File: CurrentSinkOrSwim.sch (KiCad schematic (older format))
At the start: 6 parts

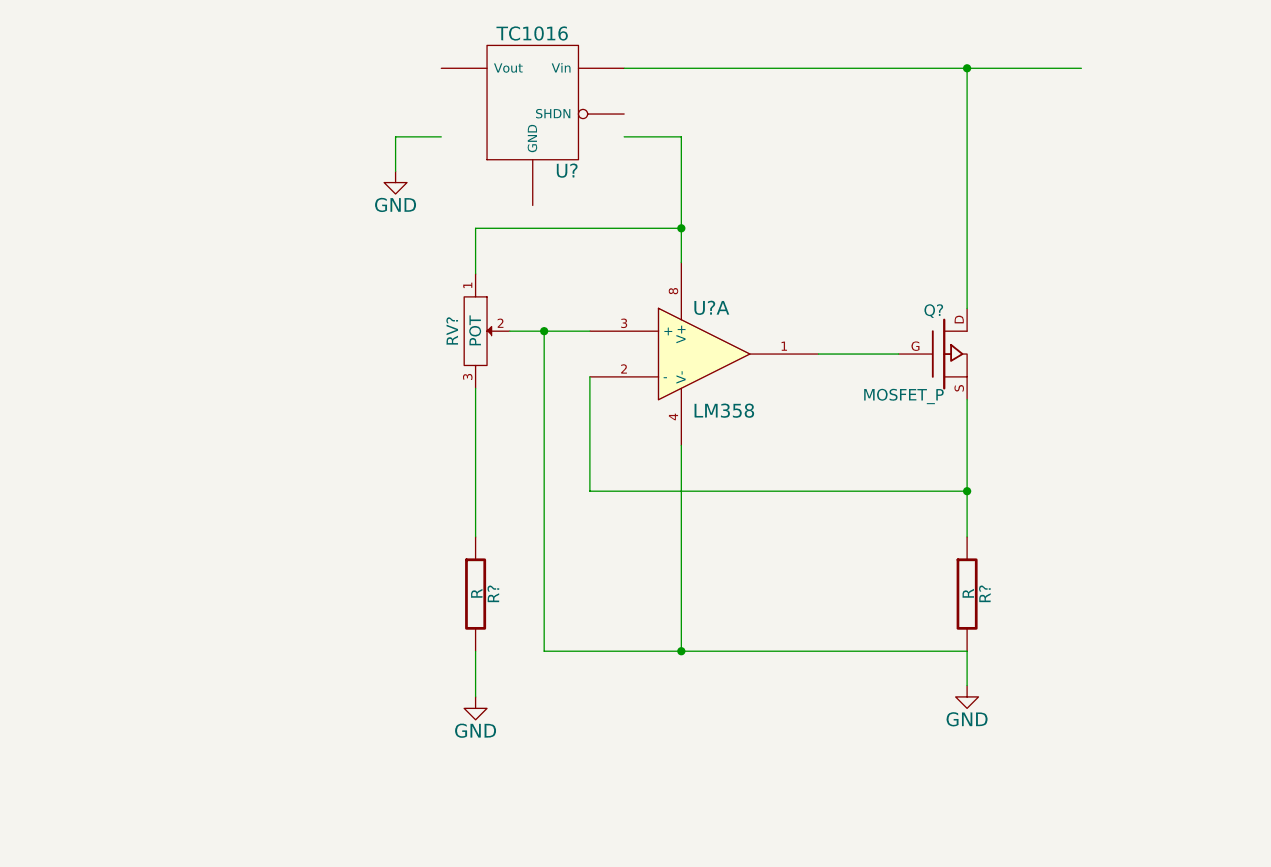
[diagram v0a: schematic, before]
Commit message: Corrections to schematic and .gitignore
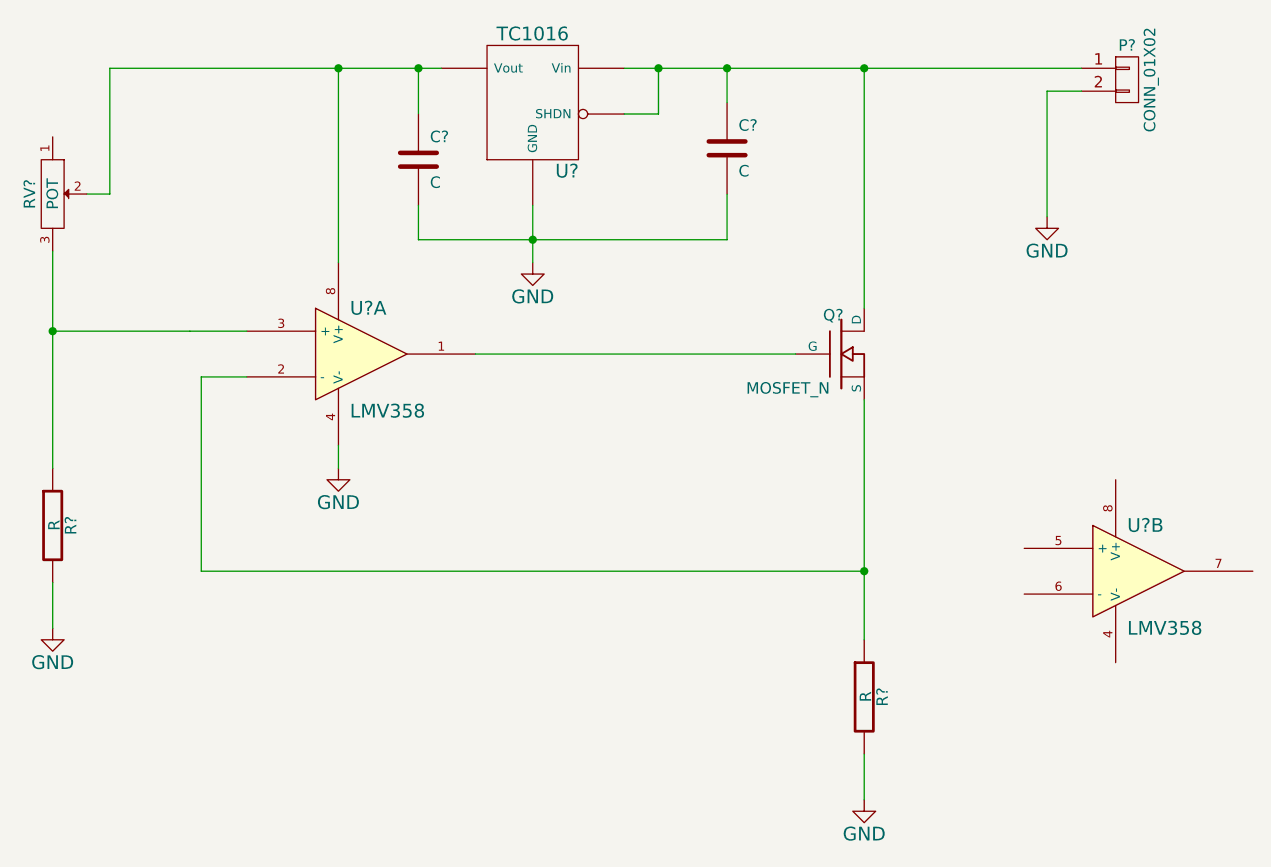
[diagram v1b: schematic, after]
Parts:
- removed Q?: MOSFET_P, symbol MOSFET_P
- removed U?: LM358, symbol LM358
- removed U?: TC1016, symbol TC1016
- added C? (x2): C, symbol C
- added P?: CONN_01X02, symbol CONN_01X02
- added Q?: MOSFET_N, symbol MOSFET_N
- added U? (x2): LMV358, symbol LMV358
- added U?: TC1016, symbol TC1016
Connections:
- wire segments 24 -> 37
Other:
- moved on the sheet: R?, RV?

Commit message: Small adjustments
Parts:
- added C?: C, symbol C
- added R?: 0, symbol R
- Q?: value MOSFET_N -> BUK9575; MPN (none) -> BUK9575-100A,127
- R?: value R -> .1; MPN (none) -> AC01000001007JA100
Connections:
- net GND: now also C?.2
- net 2.7v: now reaches C?.1, RV?.2, U?.4 (Vout), U?.8 (V+)
- net 2.7v: now also C?.1
- net at C?.1, P?.1 (P1), Q?.D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: now also R?.1; no longer U?.1 (SHDN)
- new net: R?.2, U?.1 (SHDN)
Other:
- moved on the sheet: C?, P?, R?, RV?, U?
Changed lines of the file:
@@
 L R R?
 U 1 1 54CE76B8
-P 2400 3800
-F 0 "R?" V 2480 3800 50  0000 C CNN
-F 1 "R" V 2407 3801 50  0000 C CNN
-F 2 "" V 2330 3800 30  0000 C CNN
-F 3 "" H 2400 3800 30  0000 C CNN
-	1    2400 3800
+P 2400 3850
+F 0 "R?" V 2480 3850 50  0000 C CNN
+F 1 "R" V 2407 3851 50  0000 C CNN
+F 2 "" V 2330 3850 30  0000 C CNN
+F 3 "" H 2400 3850 30  0000 C CNN
+	1    2400 3850
 	1    0    0    -1
 $EndComp
@@
 P 5950 4550
 F 0 "R?" V 6030 4550 50  0000 C CNN
-F 1 "R" V 5957 4551 50  0000 C CNN
+F 1 ".1" V 5957 4551 50  0000 C CNN
 F 2 "" V 5880 4550 30  0000 C CNN
 F 3 "" H 5950 4550 30  0000 C CNN
+F 4 "AC01000001007JA100" V 5950 4550 60  0001 C CNN "MPN"
 	1    5950 4550
 	1    0    0    -1
-$EndComp
-Wire Wire Line
-	4250 3050 5650 3050
-Wire Wire Line
-	5950 3250 5950 4000
-Wire Wire Line
-	5950 4000 5950 4300
-Wire Wire Line
-	2400 2600 2400 2950
-Wire Wire Line
-	2400 2950 2400 3550
-$Comp
-L POT RV?
-U 1 1 54CE7B4E
-P 2400 2350
-F 0 "RV?" H 2400 2250 50  0000 C CNN
-F 1 "POT" H 2400 2350 50  0000 C CNN
-F 2 "" H 2400 2350 60  0000 C CNN
-F 3 "" H 2400 2350 60  0000 C CNN
-	1    2400 2350
-	0    1    1    0
 $EndComp
 $Comp
@@
 	1    0    0    -1
 $EndComp
-Wire Wire Line
-	2400 4050 2400 4250
-Wire Wire Line
-	5950 4800 5950 5000
-Wire Wire Line
-	3050 4000 5950 4000
-Connection ~ 5950 4000
-Wire Wire Line
-	4900 1800 5050 1800
-Wire Wire Line
-	5050 1800 5350 1800
-Wire Wire Line
-	5350 1800 5950 1800
-Wire Wire Line
-	5950 1800 6900 1800
-Wire Wire Line
-	5950 1800 5950 2850
-Connection ~ 5950 1800
 $Comp
 L LMV358 U?
@@
 P 5850 3050
 F 0 "Q?" H 5860 3220 50  0000 R CNN
-F 1 "MOSFET_N" H 5800 2900 50  0000 R CNN
+F 1 "BUK9575" H 5800 2900 50  0000 R CNN
 F 2 "" H 5850 3050 60  0000 C CNN
 F 3 "" H 5850 3050 60  0000 C CNN
+F 4 "BUK9575-100A,127" H 5850 3050 60  0001 C CNN "MPN"
 	1    5850 3050
 	1    0    0    -1
@@
 	1    0    0    -1
 $EndComp
-Wire Wire Line
-	3650 3450 3650 3550
-Wire Wire Line
-	3250 3150 3050 3150
-Wire Wire Line
-	3050 3150 3050 4000
 $Comp
 L C C?
 U 1 1 54D11712
-P 5350 2150
-F 0 "C?" H 5400 2250 50  0000 L CNN
-F 1 "C" H 5400 2050 50  0000 L CNN
-F 2 "" H 5388 2000 30  0000 C CNN
-F 3 "" H 5350 2150 60  0000 C CNN
-	1    5350 2150
+P 5450 1700
+F 0 "C?" H 5500 1800 50  0000 L CNN
+F 1 "C" H 5500 1600 50  0000 L CNN
+F 2 "" H 5488 1550 30  0000 C CNN
+F 3 "" H 5450 1700 60  0000 C CNN
+	1    5450 1700
 	1    0    0    -1
 $EndComp
@@
 L C C?
 U 1 1 54D1178C
-P 4000 2200
-F 0 "C?" H 4050 2300 50  0000 L CNN
-F 1 "C" H 4050 2100 50  0000 L CNN
-F 2 "" H 4038 2050 30  0000 C CNN
-F 3 "" H 4000 2200 60  0000 C CNN
-	1    4000 2200
-	1    0    0    -1
-$EndComp
-Wire Wire Line
-	2650 1800 2650 2350
-Wire Wire Line
-	2650 2350 2550 2350
+P 4000 1750
+F 0 "C?" H 4050 1850 50  0000 L CNN
+F 1 "C" H 4050 1650 50  0000 L CNN
+F 2 "" H 4038 1600 30  0000 C CNN
+F 3 "" H 4000 1750 60  0000 C CNN
+	1    4000 1750
+	1    0    0    -1
+$EndComp
 $Comp
 L CONN_01X02 P?
 U 1 1 54D118EE
-P 7100 1850
-F 0 "P?" H 7100 2000 50  0000 C CNN
-F 1 "CONN_01X02" V 7200 1850 50  0000 C CNN
-F 2 "" H 7100 1850 60  0000 C CNN
-F 3 "" H 7100 1850 60  0000 C CNN
-	1    7100 1850
+P 6850 1400
+F 0 "P?" H 6850 1550 50  0000 C CNN
+F 1 "CONN_01X02" V 6950 1400 50  0000 C CNN
+F 2 "" H 6850 1400 60  0000 C CNN
+F 3 "" H 6850 1400 60  0000 C CNN
+	1    6850 1400
 	1    0    0    -1
 $EndComp
@@
 L TC1016 U?
 U 1 1 54D11B95
-P 4500 1850
-F 0 "U?" H 4650 1450 60  0000 C CNN
-F 1 "TC1016" H 4500 2050 60  0000 C CNN
-F 2 "" H 4500 1850 60  0000 C CNN
-F 3 "" H 4500 1850 60  0000 C CNN
-	1    4500 1850
-	1    0    0    -1
-$EndComp
-Wire Wire Line
-	2650 1800 3650 1800
-Wire Wire Line
-	3650 1800 4000 1800
-Wire Wire Line
-	4000 1800 4100 1800
-Wire Wire Line
-	3650 1800 3650 2650
-Connection ~ 3650 1800
-Wire Wire Line
-	3250 2950 3000 2950
-Wire Wire Line
-	3000 2950 3000 2950
-Wire Wire Line
-	3000 2950 2400 2950
-Connection ~ 2400 2950
+P 4500 1400
+F 0 "U?" H 4650 1000 60  0000 C CNN
+F 1 "TC1016" H 4500 1600 60  0000 C CNN
+F 2 "" H 4500 1400 60  0000 C CNN
+F 3 "" H 4500 1400 60  0000 C CNN
+	1    4500 1400
+	1    0    0    -1
+$EndComp
 $Comp
 L GND #PWR?
 U 1 1 54D11EA4
-P 4500 2650
-F 0 "#PWR?" H 4500 2400 60  0001 C CNN
-F 1 "GND" H 4500 2500 60  0000 C CNN
-F 2 "" H 4500 2650 60  0000 C CNN
-F 3 "" H 4500 2650 60  0000 C CNN
-	1    4500 2650
-	1    0    0    -1
-$EndComp
-Wire Wire Line
-	4500 2400 4500 2550
-Wire Wire Line
-	4500 2550 4500 2650
-Wire Wire Line
-	5350 1800 5350 1950
-Connection ~ 5350 1800
-Wire Wire Line
-	5350 2550 5350 2350
-Connection ~ 4500 2550
-Wire Wire Line
-	4000 1800 4000 2000
-Connection ~ 4000 1800
-Wire Wire Line
-	4000 2400 4000 2550
-Wire Wire Line
-	4900 2000 5050 2000
-Wire Wire Line
-	5050 2000 5050 1800
-Connection ~ 5050 1800
+P 4500 2200
+F 0 "#PWR?" H 4500 1950 60  0001 C CNN
+F 1 "GND" H 4500 2050 60  0000 C CNN
+F 2 "" H 4500 2200 60  0000 C CNN
+F 3 "" H 4500 2200 60  0000 C CNN
+	1    4500 2200
+	1    0    0    -1
+$EndComp
 $Comp
 L GND #PWR?
 U 1 1 54D120EF
-P 6750 2450
-F 0 "#PWR?" H 6750 2200 60  0001 C CNN
-F 1 "GND" H 6750 2300 60  0000 C CNN
-F 2 "" H 6750 2450 60  0000 C CNN
-F 3 "" H 6750 2450 60  0000 C CNN
-	1    6750 2450
-	1    0    0    -1
-$EndComp
-Wire Wire Line
-	6750 1900 6750 2450
-Wire Wire Line
-	6750 1900 6900 1900
-Wire Wire Line
-	4000 2550 4500 2550
-Wire Wire Line
-	4500 2550 5350 2550
+P 6550 2450
+F 0 "#PWR?" H 6550 2200 60  0001 C CNN
+F 1 "GND" H 6550 2300 60  0000 C CNN
+F 2 "" H 6550 2450 60  0000 C CNN
+F 3 "" H 6550 2450 60  0000 C CNN
+	1    6550 2450
+	1    0    0    -1
+$EndComp
+$Comp
+L R R?
+U 1 1 54D915F0
+P 5150 1700
+F 0 "R?" V 5230 1700 50  0000 C CNN
+F 1 "0" V 5157 1701 50  0000 C CNN
+F 2 "" V 5080 1700 30  0000 C CNN
+F 3 "" H 5150 1700 30  0000 C CNN
+F 4 "Value" H 5150 1700 60  0001 C CNN "MPN"
+	1    5150 1700
+	1    0    0    -1
+$EndComp
+$Comp
+L C C?
+U 1 1 54D91774
+P 3250 2350
+F 0 "C?" H 3300 2450 50  0000 L CNN
+F 1 "C" H 3300 2250 50  0000 L CNN
+F 2 "" H 3288 2200 30  0000 C CNN
+F 3 "" H 3250 2350 60  0000 C CNN
+	1    3250 2350
+	1    0    0    -1
+$EndComp
+Wire Wire Line
+	4250 3050 5650 3050
+Wire Wire Line
+	5950 3250 5950 4000
+Wire Wire Line
+	5950 4000 5950 4300
+Wire Wire Line
+	2400 3400 2400 3500
+Wire Wire Line
+	2400 3500 2400 3600
+Wire Wire Line
+	2400 4100 2400 4250
+Wire Wire Line
+	5950 4800 5950 5000
+Wire Wire Line
+	3050 4000 5950 4000
+Connection ~ 5950 4000
+Wire Wire Line
+	4900 1350 5150 1350
+Wire Wire Line
+	5150 1350 5450 1350
+Wire Wire Line
+	5450 1350 5950 1350
+Wire Wire Line
+	5950 1350 6650 1350
+Wire Wire Line
+	5950 1350 5950 2850
+Connection ~ 5950 1350
+Wire Wire Line
+	3650 3450 3650 3550
+Wire Wire Line
+	3250 3150 3050 3150
+Wire Wire Line
+	3050 3150 3050 4000
+Wire Wire Line
+	2650 1350 4000 1350
+Wire Wire Line
+	4000 1350 4100 1350
+Wire Wire Line
+	4500 1950 4500 2100
+Wire Wire Line
+	4500 2100 4500 2200
+Wire Wire Line
+	5450 1350 5450 1500
+Connection ~ 5450 1350
+Wire Wire Line
+	5450 2100 5450 1900
+Connection ~ 4500 2100
+Wire Wire Line
+	4000 1350 4000 1550
+Connection ~ 4000 1350
+Wire Wire Line
+	4000 1950 4000 2100
+Wire Wire Line
+	6550 1450 6550 2450
+Wire Wire Line
+	6550 1450 6650 1450
+Wire Wire Line
+	4000 2100 4500 2100
+Wire Wire Line
+	4500 2100 5450 2100
+Wire Wire Line
+	5150 1450 5150 1350
+Connection ~ 5150 1350
+Wire Wire Line
+	5150 1950 5150 2000
+Wire Wire Line
+	5150 2000 4950 2000
+Wire Wire Line
+	4950 2000 4950 1550
+$Comp
+L POT RV?
+U 1 1 54CE7B4E
+P 2400 3150
+F 0 "RV?" H 2400 3050 50  0000 C CNN
+F 1 "POT" H 2400 3150 50  0000 C CNN
+F 2 "" H 2400 3150 60  0000 C CNN
+F 3 "" H 2400 3150 60  0000 C CNN
+	1    2400 3150
+	0    1    1    0
+$EndComp
+Wire Wire Line
+	2650 3150 2550 3150
+Wire Wire Line
+	2650 1350 2650 2050
+Wire Wire Line
+	2650 2050 2650 3150
+Wire Wire Line
+	3650 2050 3650 2650
+Wire Wire Line
+	2650 2050 3250 2050
+Wire Wire Line
+	3250 2050 3650 2050
+Connection ~ 2650 2050
+Text Label 3000 2050 0    60   ~ 0
+2.7v
+Wire Wire Line
+	3250 2150 3250 2050
+Connection ~ 3250 2050
+$Comp
+L GND #PWR?
+U 1 1 54D91D18
+P 3250 2650
+F 0 "#PWR?" H 3250 2400 60  0001 C CNN
+F 1 "GND" H 3250 2500 60  0000 C CNN
+F 2 "" H 3250 2650 60  0000 C CNN
+F 3 "" H 3250 2650 60  0000 C CNN
+	1    3250 2650
+	1    0    0    -1
+$EndComp
+Wire Wire Line
+	3250 2650 3250 2550
+Wire Wire Line
+	3250 2950 2850 2950
+Wire Wire Line
+	2850 2950 2850 3500
+Wire Wire Line
+	2850 3500 2400 3500
+Connection ~ 2400 3500
+Wire Wire Line
+	4950 1550 4900 1550
 $EndSCHEMATC

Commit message: Caught up with video 18 - Linear Regulator
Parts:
- removed U?: TC1016, symbol TC1016
- added P?: CONN_01X03, symbol CONN_01X03
- added P?: CONN_01X02, symbol CONN_01X02
- added R?: 27k, symbol R
- added R?: 21.6k, symbol R
- added U?: LM2931D-R, symbol LM2931D-R
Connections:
- wire segments 44 -> 64
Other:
- note added: "Battery pack\n"
- note added: "Current sink input"
- moved on the sheet: C?, P?, Q?, R?, RV?, U?A, U?B

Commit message: Adding hierarchical sheets and voltage control circuit - Catching up with video 21
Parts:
- removed C? (x3): C, symbol C
- removed Q?: BUK9575, symbol MOSFET_N
- removed R?: R, symbol R
- removed R?: .1, symbol R
- removed R?: 0, symbol R
- removed R?: 27k, symbol R
- removed R?: 21.6k, symbol R
- removed RV?: POT, symbol POT
- removed U? (x2): LMV358, symbol LMV358
- removed U?: LM2931D-R, symbol LM2931D-R
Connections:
- net labels removed: 2.7v
- wire segments 64 -> 21
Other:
- moved on the sheet: P?

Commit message: Small correction
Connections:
- wire segments 21 -> 17
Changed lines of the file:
@@
 $EndComp
 Wire Wire Line
-	5350 1550 5350 2350
+	5350 1550 5350 5550
 Wire Wire Line
-	5350 2350 5350 3600
-Wire Wire Line
-	5350 3600 5350 5550
-Wire Wire Line
-	5900 2450 5900 4150
-Wire Wire Line
-	5900 4150 5900 5950
-Wire Wire Line
-	5900 5950 5900 6550
+	5900 2450 5900 6550
 Wire Wire Line
 	5900 2450 6050 2450

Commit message: Initial annotation
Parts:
- P101: renamed from P?; footprint (none) -> Pin_Headers:Pin_Header_Straight_1x03
- P102, P103: renamed from P?; footprint (none) -> Pin_Headers:Pin_Header_Straight_1x02
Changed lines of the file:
@@
 $EndDescr
 $Comp
-L CONN_01X02 P?
+L CONN_01X02 P103
 U 1 1 54D118EE
 P 6250 2400
-F 0 "P?" H 6250 2550 50  0000 C CNN
+F 0 "P103" H 6250 2550 50  0000 C CNN
 F 1 "CONN_01X02" V 6350 2400 50  0000 C CNN
-F 2 "" H 6250 2400 60  0000 C CNN
+F 2 "Pin_Headers:Pin_Header_Straight_1x02" H 6250 2400 60  0001 C CNN
 F 3 "" H 6250 2400 60  0000 C CNN
 	1    6250 2400
@@
 	5350 2350 6050 2350
 $Comp
-L CONN_01X03 P?
+L CONN_01X03 P101
 U 1 1 54E39144
 P 5250 1350
-F 0 "P?" H 5250 1550 50  0000 C CNN
+F 0 "P101" H 5250 1550 50  0000 C CNN
 F 1 "CONN_01X03" V 5350 1350 50  0000 C CNN
-F 2 "" H 5250 1350 60  0000 C CNN
+F 2 "Pin_Headers:Pin_Header_Straight_1x03" H 5250 1350 60  0001 C CNN
 F 3 "" H 5250 1350 60  0000 C CNN
 	1    5250 1350
@@
 Connection ~ 5350 2350
 $Comp
-L CONN_01X02 P?
+L CONN_01X02 P102
 U 1 1 54E39227
 P 2350 1700
-F 0 "P?" H 2350 1850 50  0000 C CNN
+F 0 "P102" H 2350 1850 50  0000 C CNN
 F 1 "CONN_01X02" V 2450 1700 50  0000 C CNN
-F 2 "" H 2350 1700 60  0000 C CNN
+F 2 "Pin_Headers:Pin_Header_Straight_1x02" H 2350 1700 60  0001 C CNN
 F 3 "" H 2350 1700 60  0000 C CNN
 	1    2350 1700

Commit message: Preliminary footprint association
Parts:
- P101: footprint Pin_Headers:Pin_Header_Straight_1x03 -> Pin_Headers:Pin_Header_Angled_1x03
- P102, P103: footprint Pin_Headers:Pin_Header_Straight_1x02 -> Pin_Headers:Pin_Header_Angled_1x02
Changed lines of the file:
@@
 F 0 "P103" H 6250 2550 50  0000 C CNN
 F 1 "CONN_01X02" V 6350 2400 50  0000 C CNN
-F 2 "Pin_Headers:Pin_Header_Straight_1x02" H 6250 2400 60  0001 C CNN
+F 2 "Pin_Headers:Pin_Header_Angled_1x02" H 6250 2400 60  0001 C CNN
 F 3 "" H 6250 2400 60  0000 C CNN
 	1    6250 2400
@@
 F 0 "P101" H 5250 1550 50  0000 C CNN
 F 1 "CONN_01X03" V 5350 1350 50  0000 C CNN
-F 2 "Pin_Headers:Pin_Header_Straight_1x03" H 5250 1350 60  0001 C CNN
+F 2 "Pin_Headers:Pin_Header_Angled_1x03" H 5250 1350 60  0001 C CNN
 F 3 "" H 5250 1350 60  0000 C CNN
 	1    5250 1350
@@
 F 0 "P102" H 2350 1850 50  0000 C CNN
 F 1 "CONN_01X02" V 2450 1700 50  0000 C CNN
-F 2 "Pin_Headers:Pin_Header_Straight_1x02" H 2350 1700 60  0001 C CNN
+F 2 "Pin_Headers:Pin_Header_Angled_1x02" H 2350 1700 60  0001 C CNN
 F 3 "" H 2350 1700 60  0000 C CNN
 	1    2350 1700

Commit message: Updated the POT references and schematic
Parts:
- P101: footprint Pin_Headers:Pin_Header_Angled_1x03 -> Pin_Headers:Pin_Header_Straight_1x03
- P102, P103: footprint Pin_Headers:Pin_Header_Angled_1x02 -> CSOS Local:Terminal_Block_1x200_mil
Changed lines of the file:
@@
 P 6250 2400
 F 0 "P103" H 6250 2550 50  0000 C CNN
-F 1 "CONN_01X02" V 6350 2400 50  0000 C CNN
-F 2 "Pin_Headers:Pin_Header_Angled_1x02" H 6250 2400 60  0001 C CNN
+F 1 "CONN_01X02" V 6350 2400 50  0001 C CNN
+F 2 "CSOS Local:Terminal_Block_1x200_mil" H 6250 2400 60  0001 C CNN
 F 3 "" H 6250 2400 60  0000 C CNN
 	1    6250 2400
@@
 Wire Wire Line
 	5900 2450 5900 6550
-Wire Wire Line
-	5900 2450 6050 2450
-Wire Wire Line
-	5350 2350 6050 2350
 $Comp
 L CONN_01X03 P101
@@
 P 5250 1350
 F 0 "P101" H 5250 1550 50  0000 C CNN
-F 1 "CONN_01X03" V 5350 1350 50  0000 C CNN
-F 2 "Pin_Headers:Pin_Header_Angled_1x03" H 5250 1350 60  0001 C CNN
+F 1 "CONN_01X03" V 5350 1350 50  0001 C CNN
+F 2 "Pin_Headers:Pin_Header_Straight_1x03" H 5250 1350 60  0001 C CNN
 F 3 "" H 5250 1350 60  0000 C CNN
 	1    5250 1350
@@
 P 2350 1700
 F 0 "P102" H 2350 1850 50  0000 C CNN
-F 1 "CONN_01X02" V 2450 1700 50  0000 C CNN
-F 2 "Pin_Headers:Pin_Header_Angled_1x02" H 2350 1700 60  0001 C CNN
+F 1 "CONN_01X02" V 2450 1700 50  0001 C CNN
+F 2 "CSOS Local:Terminal_Block_1x200_mil" H 2350 1700 60  0001 C CNN
 F 3 "" H 2350 1700 60  0000 C CNN
 	1    2350 1700
-	-1   0    0    1
+	-1   0    0    -1
 $EndComp
 Wire Wire Line
@@
 	1    0    0    -1
 $EndComp
-Text Notes 2050 2050 0    60   ~ 0
+Text Notes 2000 1950 0    60   ~ 0
 Battery pack\n
-Text Notes 6050 2750 0    60   ~ 0
+Text Notes 6050 2650 0    60   ~ 0
 Current sink input
 $Sheet
@@
 Wire Wire Line
 	5250 2150 4900 2150
+Wire Wire Line
+	5350 2350 6050 2350
+Wire Wire Line
+	5900 2450 6050 2450
 $EndSCHEMATC
